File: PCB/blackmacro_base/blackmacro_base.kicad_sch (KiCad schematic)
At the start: 128 parts, among them J1 MOD Power, J2 MOD I/O, J3 Dial_PowerConn, J4 Dial_MagEncoderConn, J5 Dial_MotorControlConn, U1 TP4056-42-ESOP8, U2 74HC238, U3 SN74LVC1T45DBV

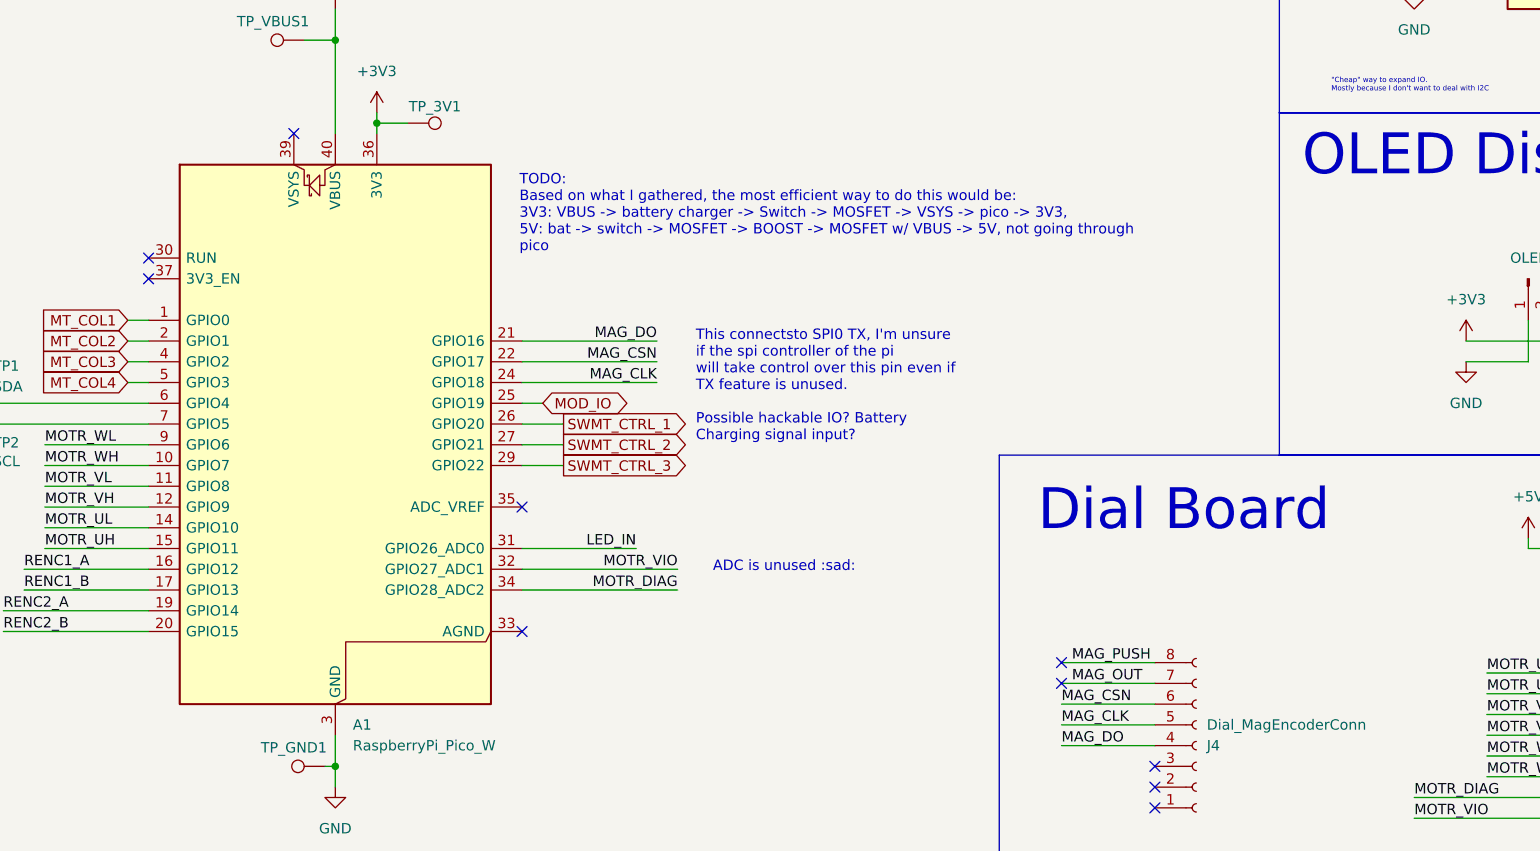
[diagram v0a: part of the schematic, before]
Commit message: updated pico footprint for pcb usb connections
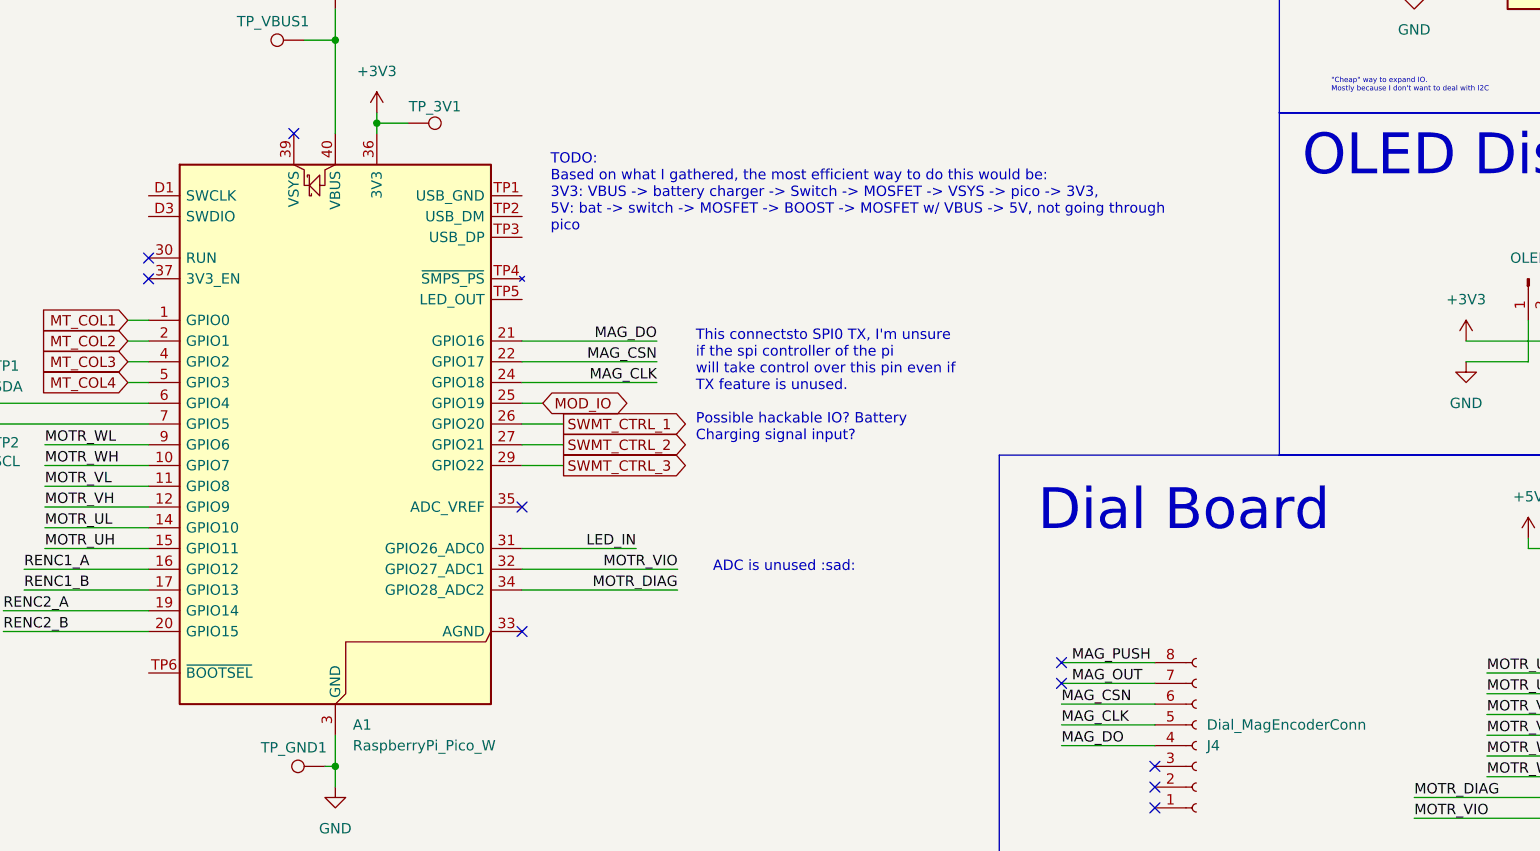
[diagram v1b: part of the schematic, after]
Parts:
- A1: footprint Module:RaspberryPi_Pico_W_SMD_HandSolder -> Module:RaspberryPi_Pico_W_SMD; symbol MCU_Module:RaspberryPi_Pico_W -> MCU_Module:RaspberryPi_Pico_W_Extensive
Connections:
- net GND: now also A1.D2 (GND)
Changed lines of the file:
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@@
 	(text_box "TODO:\nBased on what I gathered, the most efficient way to do this would be:\n3V3: VBUS -> battery charger -> Switch -> MOSFET -> VSYS -> pico -> 3V3,\n5V: bat -> switch -> MOSFET -> BOOST -> MOSFET w/ VBUS -> 5V, not going through pico"
 		(exclude_from_sim no)
-		(at 92.71 120.65 0)
+		(at 96.52 118.11 0)
 		(size 91.44 16.2161)
 		(margins 0.9525 0.9525 0.9525 0.9525)
@@
 	)
 	(symbol
-		(lib_id "MCU_Module:RaspberryPi_Pico_W")
+		(lib_id "MCU_Module:RaspberryPi_Pico_W_Extensive")
 		(at 71.12 154.94 0)
 		(unit 1)
@@
 			)
 		)
-		(property "Footprint" "Module:RaspberryPi_Pico_W_SMD_HandSolder"
+		(property "Footprint" "Module:RaspberryPi_Pico_W_SMD"
 			(at 71.12 201.93 0)
 			(hide yes)
@@
 			)
 		)
-		(property "Description" "Versatile and inexpensive wireless microcontroller module powered by RP2040 dual-core Arm Cortex-M0+ processor up to 133 MHz, 264kB SRAM, 2MB QSPI flash, Infineon CYW43439 2.4GHz 802.11n wireless LAN; also supports Raspberry Pi Pico 2 W"
+		(property "Description" "Versatile and inexpensive wireless microcontroller module (with full pinout for test point and debug connections) powered by RP2040 dual-core Arm Cortex-M0+ processor up to 133 MHz, 264kB SRAM, 2MB QSPI flash, Infineon CYW43439 2.4GHz 802.11n wireless LAN; also supports Raspberry Pi Pico 2 W"
 			(at 71.12 207.01 0)
 			(hide yes)
@@
 		(pin "40"
 		)
-		(pin "39"
+		(pin "D2"
 		)
 		(pin "13"
@@
 		(pin "34"
 		)
+		(pin "D1"
+		)
+		(pin "39"
+		)
+		(pin "TP6"
+		)
+		(pin "TP4"
+		)
+		(pin "TP5"
+		)
+		(pin "TP2"
+		)
+		(pin "TP3"
+		)
+		(pin "D3"
+		)
+		(pin "TP1"
+		)
 		(instances

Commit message: switched to pcb usb socket, battery management wip switched to pouch instead of 16850 pcb ready for rewiring + keyboard adjustments
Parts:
- removed H1, H2, H3, H4, H5, H6: MountingHole, MountingHole:MountingHole_3.2mm_M3_ISO14580_Pad, symbol Mechanical:MountingHole
- added J6: USB_C_Receptacle_USB2.0_16P, Connector_USB:USB_C_Receptacle_HCTL_HC-TYPE-C-16P-01A, symbol Connector:USB_C_Receptacle_USB2.0_16P
- added JP1: ChargeSigJumper, Jumper:SolderJumper-2_P1.3mm_Open_TrianglePad1.0x1.5mm, symbol Jumper:SolderJumper_2_Open
- added R10, R11: 5.1k, Resistor_SMD:R_0603_1608Metric_Pad0.98x0.95mm_HandSolder, symbol Device:R
- added R9: 1.2k, Resistor_SMD:R_0805_2012Metric_Pad1.20x1.40mm_HandSolder, symbol Device:R_Small
- added TH1: 10k, 43C=4.791k, Connector_Wire:SolderWire-0.127sqmm_1x02_P3.7mm_D0.48mm_OD1mm_Relief, symbol Device:Thermistor_NTC
- added U4: BQ27427, Package_SON:Texas_S-PDSO-N12, symbol PCM_marbastlib-various:BQ27427
- BT1: value FLY18650-3500mAh-3.6V -> FLY.906090.6000; footprint Battery:BatteryHolder_Keystone_1042_1x18650 -> Connector_JST:JST_EH_S3B-EH_1x03_P2.50mm_Horizontal; now fitted; now in the parts list
- C1, C2, R1: now fitted; now in the parts list
- DB1, DB2, R2, R3: now in the parts list
- J2: footprint Connector_PinSocket_2.54mm:PinSocket_1x03_P2.54mm_Horizontal -> Connector_PinSocket_2.54mm:PinSocket_1x02_P2.54mm_Horizontal; symbol Connector:Conn_01x03_Socket -> Connector:Conn_01x02_Socket
- R4: value 1.74k -> 1.2k; footprint (none) -> Resistor_SMD:R_0805_2012Metric_Pad1.20x1.40mm_HandSolder; now fitted; now in the parts list
- U1: value TP4056-42-ESOP8 -> HTP4056-42-ESOP8; symbol Battery_Management:TP4056-42-ESOP8 -> custom:HTP4056-42-ESOP8; now fitted; now in the parts list
- renumbered TP_VBUS1 to TP_VSYS
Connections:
- net +5V: now also A1.39 (VSYS); no longer A1.40 (VBUS)
- net GND: now also J6.A1 (GND), J6.A12 (GND), J6.B1 (GND), J6.B12 (GND), J6.SH (SHIELD), R10.2, R11.2, TH1.2; no longer BT1.2 (-)
- net MOD_O1: now also J2.1 (Pin_1); no longer J2.2 (Pin_2)
- net MOD_O2: now also J2.2 (Pin_2); no longer J2.3 (Pin_3)
- net VBUS: now also J6.A4 (VBUS), J6.A9 (VBUS), J6.B4 (VBUS), J6.B9 (VBUS)
- net at C2.1, R1.2, R2.1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: no longer U1.8 (CE)
- net SRX: now reaches C1.1, U1.5 (BAT)
- net SRX: now also R9.2, U4.C2 (SRX); no longer BT1.1 (+)
- net at U1.1 (TEMP): now also R9.1, TH1.1
- net at DB2.1 (K), U1.7 (~{CHRG}): now also JP1.1 (A)
- net MOD_IO renamed CHRG
- net CHRG: now also JP1.2 (B); no longer J2.1 (Pin_1)
- new net: J6.B5 (CC2), R10.1
- new net: BT1.1 (+), U4.C3 (BAT)
- new net: J6.A5 (CC1), R11.1
- new net: J6.A6 (D+), J6.B6 (D+)
- new net: J6.A7 (D-), J6.B7 (D-)
- new net Vss: U4.B2 (Vss), U4.C1 (Vss)
- no-connect marks 40 -> 44
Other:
- note added: "Battery Charging"
- note added: "Fuel Gauge"
- note added: "TEMP SENSING"
- note added: "UPDATE: I'm using a pouch cell now! It has a built-in protection circuit, so a BMS is omitted here. Make sure you're also buying pouch cells with a builtin protection circuit! I'm using HTP4056 here w/ 1.2A max. Another option would be TP5000X which would allow much higher charging current, but brings too much complexity (switching instead of ldo) that it's not really worth it imo."
- note added: "Unfortunately it's a BGA chip. It's also quite expensive :("
- note removed: "Battery (TODO)"
- note removed: "I'm using a 18650 with BUILT-IN BMS. So BMS circuit is omitted here. Make sure you're also buying 18650s with built in protection circuits, or add a BMS here!"
- note removed: "TODO: TEMP SENSING"
- note removed: "V1 does not include battery support!"
- moved on the sheet: A1, C3, DB1, DB2, J1, J3, J4, J5, LED1, LED10, LED11, LED12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

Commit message: just the schottky diode left.... the BOM has now grown to 100 cny.... man this thing is gonna be expensive...
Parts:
- added C13, C17: 22uF, Capacitor_SMD:C_0603_1608Metric_Pad1.08x0.95mm_HandSolder, symbol Device:C
- added C14, C18: 0.1uF, Capacitor_SMD:C_1206_3216Metric_Pad1.33x1.80mm_HandSolder, symbol Device:C_Small
- added C15, C16: 3.3uF, Capacitor_SMD:C_0603_1608Metric_Pad1.08x0.95mm_HandSolder, symbol Device:C_Small
- added L1: 4.7uH, Inductor_SMD:L_Changjiang_FXL0630, symbol Device:L
- added Q1, Q2: AO3415, Package_TO_SOT_SMD:SOT-23_Handsoldering, symbol custom:AO3415
- added R12, R13: 8.2k, Resistor_SMD:R_0805_2012Metric_Pad1.20x1.40mm_HandSolder, symbol Device:R_Small
- added R14: 5.1k, Resistor_SMD:R_0603_1608Metric_Pad0.98x0.95mm_HandSolder, symbol Device:R
- added R15: 37.4k, Resistor_SMD:R_0603_1608Metric_Pad0.98x0.95mm_HandSolder, symbol Device:R
- added SW1: SW_SPDT, Button_Switch_SMD:SW_SPDT_Shouhan_MSK12C02, symbol Switch:SW_SPDT
- added TP_VBUS: VBUS test point, TestPoint:TestPoint_THTPad_D1.5mm_Drill0.7mm, symbol Connector:TestPoint
- added U5: MT3608L, Package_TO_SOT_SMD:SOT-23-6_Handsoldering, symbol custom:MT3608L
- TP_3V3: renamed from TP_3V1; value VSYS test point -> 3V3 test point
- TP_GND: renamed from TP_GND1; value VSYS test point -> GND test point
- U4: footprint Package_SON:Texas_S-PDSO-N12 -> Package_BGA:Texas_DSBGA-9_1.62x1.58mm_Layout3x3_P0.5mm
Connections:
- net Vss is gone; now on net GND: U4.B2 (Vss), U4.C1 (Vss)
- net +5V: no longer A1.39 (VSYS), TP_VSYS.1
- net GND: now also A1.TP1 (USB_GND), BT1.2 (-), C13.2, C14.1, C15.2, C16.2, C17.2, C18.1, R12.1, R14.1, U5.2 (GND)
- net MOD_O2: now also U2.7 (Y7); no longer U2.10 (Y5)
- net MT_ROW1: now also U2.15 (Y0); no longer U2.11 (Y4)
- net MT_ROW2: now also U2.14 (Y1); no longer U2.12 (Y3)
- net MT_ROW4: now also U2.12 (Y3); no longer U2.14 (Y1)
- net MT_ROW5: now also U2.11 (Y4); no longer U2.15 (Y0)
- net MT_ROW6: now also U2.10 (Y5); no longer U2.7 (Y7)
- net SCL: now also U4.A3 (SCL)
- net SDA: now also U4.A2 (SDA)
- net SRX: now also SW1.2 (B)
- net VBUS: now also A1.40 (VBUS), C18.2, Q1.1 (G), Q2.1 (G), TP_VBUS.1
- net at BT1.1 (+), U4.C3 (BAT): now also C16.1
- net at U4.A1 (GPOUT): now also R13.2
- net at U4.B1 (BIN): now also R12.2
- net at U4.B3 (Vdd): now also C15.1, R13.1
- net USB_D-: now reaches A1.TP2 (USB_DM)
- net USB_D-: now also J6.A7 (D-), J6.B7 (D-)
- net USB_D+: now reaches A1.TP3 (USB_DP)
- net USB_D+: now also J6.A6 (D+), J6.B6 (D+)
- new net: R14.2, R15.2, U5.3 (FB)
- new net: L1.2, U5.1 (SW)
- new net BATT_5V: C13.1, R15.1
- new net BOOST_IN: C17.1, L1.1, Q2.2 (S), U5.4 (EN), U5.5 (IN)
- new net VBAT: C14.2, Q1.3 (D), Q2.3 (D), SW1.1 (A)
- new net VSYS: A1.39 (VSYS), Q1.2 (S), TP_VSYS.1
- no-connect marks 44 -> 46
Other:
- note added: "Battery 5V boost"
- note added: "Currently this chip won't shutdown since it's always powered by the battery. connect gpout to GPIO for software controlled shutdown+wakeup"
- note added: "Defaults to 2.5A limit"
- note added: "Maybe add a PPTC here. ~2A hold 3~4A trip should be okay"
- note added: "Maybe replace with schottky diodes instead? shave a couple bucks off"
- note added: "Moddable switch"
- note added: "ON as long as there's power"
- note added: "Power Handoff"
- note added: "TODO: Schottky diode"
- note added: "USB"
- note added: "VBUS is USB only (5V) VSYS is either USB 5V, or battery ~3.7V. Dedicated 5V is separate. 3.3V is from pico and stable in both conditions"
- note added: "debounce."
- note added: "mosfet pulldown not required, builtin of the pico"
- note added: "okay, SO, Looking at TI's datasheet, The block diagram plus the application circuit shows this being 1uF, BUT in the recommended operating conditions chart it's 0.1uF. Capacitor prices are through the roof right now for some dumb fucking reason, so i'm not buying new caps if i dont have to. I'm gonna use a 3.3uF for this and vdd since it's cheaper lol"
- note removed: "Hackable switch"
- note removed: "TODO: Add battery management"
- moved on the sheet: A1, BT1, C1, C2, C3, DB1, DB2, J1, J2, J6, JP1, LED1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
